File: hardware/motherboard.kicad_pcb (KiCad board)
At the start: 2 copper layers, 200 x 150 mm, 318 parts, among them J1 24 V DC input, J10 AX0: EN, STEP, DIR, GND, J11 AX1: EN, STEP, DIR, GND, J12 General outputs 0-7; pin9 fie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, J13 Encoder 0: +5,A,B,Z,GND, J14 Encoder 1: +5,A,B,Z,GND, J15 Encoder 2: +5,A,B,Z,GND, J16 Keyboard KIN0-7 / KOUT0-7, J17 Keyboard power/reference, J18 I2C0, J19 Full-size SD, SPI, J2 Backlight: +12V, GND, PWM, sw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, J20 ESP-01S socket, J22 LCD LVDS 2x10, 2.00 mm, J24 AI0/GND/AI1/GND/AI2/GND, J25 0-10 V outputs 0-3; pin 1 = c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, J26 Dedicated START button input, J27 Expansion inputs 4-7; 1=GND, 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, J28 AX2: EN, STEP, DIR, GND, J29 AX3: EN, STEP, DIR, GND, J30 AX4: EN, STEP, DIR, GND, J31 Motion AUX open-drain output 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, J32 General outputs 8-15; DO_COM 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, J33 General outputs field +V and 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, J34 PLC positions 5-8 of J7 bank;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, J35 PLC positions 5-8 of J8 bank;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, J4 SWD, J5 Dedicated E-stop loop, J6 Dedicated HOLD button input, J7 PLC inputs 1-8; alternating i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, J8 PLC inputs 9-16; alternating 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, J9 Expansion inputs 0-3; 1=GND, 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, Q5 BSS138, Q6 BSS138, Q7 BSS138, Q8 BSS138, SW2 ESP_PROG, U1 LMR36510ADDAR, U10 74HC595D, U11 74HC595D, U12 74HC595D, U13 74HC595D, U18 LTV-847S, U19 LTV-847S, U2 AMS1117-3.3, U20 LTV-847S, U21 LTV-847S, U24 SN74AHCT541DW, U25 SN74AHCT541DW, U26 ULN2003ADR, U27 ULN2003ADR, U28 SN74AHCT541DW, U3 LMR36510ADDAR, U34 AMS1117-3.3, U35 EL3H7, U36 EL3H7, U37 L78L12ACUTR, U38 TLV2374IDR, U39 EL3H7, U40 TBA2-0512, U41 DS90LV047A, U6 74HC165D, U7 74HC165D, U8 74HC165D, U9 74HC165D

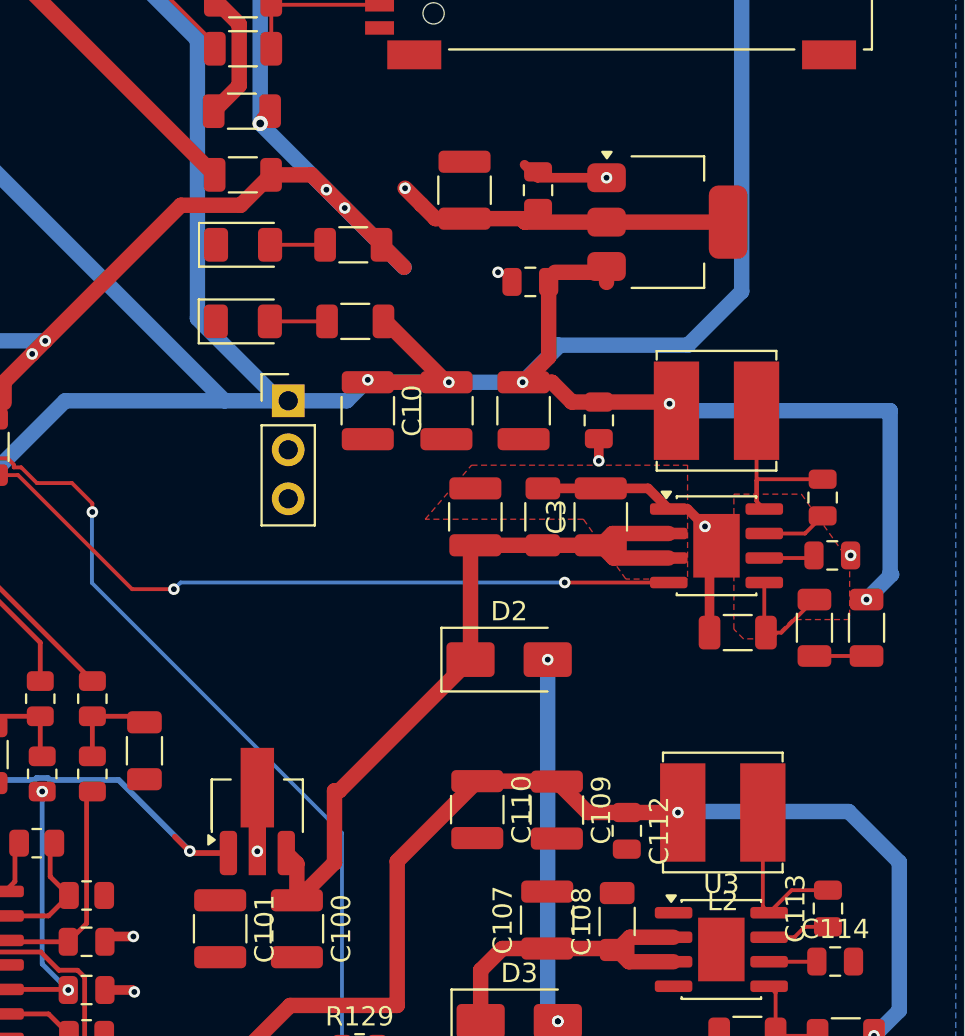
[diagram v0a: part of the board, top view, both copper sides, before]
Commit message: Close final PCB connectivity gaps
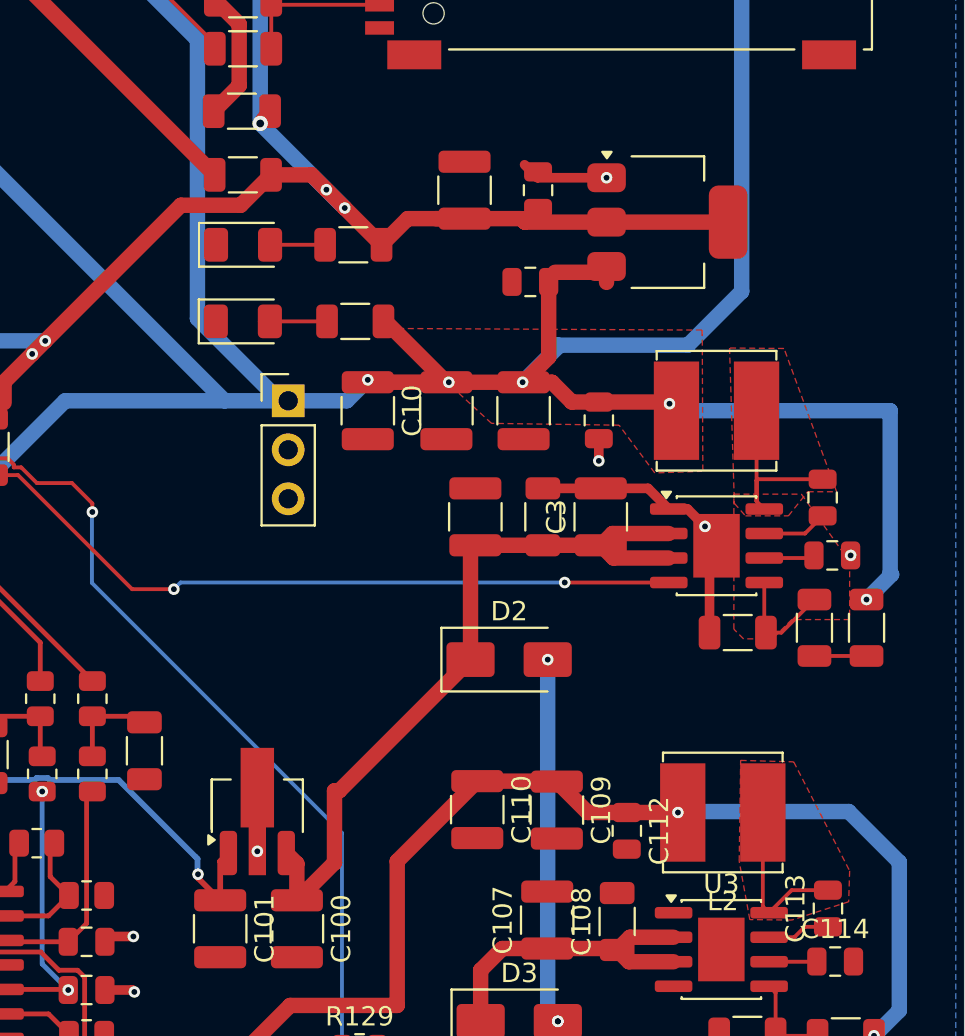
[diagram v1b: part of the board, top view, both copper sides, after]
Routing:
- net +3V3: track 678.7 -> 675.3 mm, vias 29 -> 28
- net +12V_AO: track 26.6 -> 29.4 mm
- net GND: vias 92 -> 91
- added copper zone on F.Cu, net BUCK12_SW
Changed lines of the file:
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@@
 	)
 	(via
-		(at 175.775 93.5)
-		(size 0.6)
-		(drill 0.3)
-		(layers "F.Cu" "B.Cu")
-		(net "GND")
-	)
-	(via
 		(at 157.85 47.9)
 		(size 0.6)
@@
 	)
 	(segment
+		(start 173.225 99.2)
+		(end 177.05 99.2)
+		(width 0.8)
+		(layer "F.Cu")
+		(net "+5V")
+	)
+	(segment
 		(start 173.1 99.2)
 		(end 173.225 99.2)
@@
 	)
 	(segment
-		(start 177.05 99.2)
-		(end 173.225 99.2)
-		(width 0.8)
-		(layer "B.Cu")
-		(net "+5V")
-	)
-	(segment
 		(start 161.6 100.16)
 		(end 153.34 100.16)
@@
 	)
 	(segment
-		(start 159.025 122.75)
-		(end 159.875 123.6)
+		(start 160.225 124.9)
+		(end 161.375 126.05)
 		(width 0.3)
 		(layer "F.Cu")
@@
 	)
 	(segment
-		(start 159.875 123.6)
+		(start 161.375 124.025)
 		(end 161.8 123.6)
 		(width 0.3)
@@
 	)
 	(segment
+		(start 160.225 124.7)
+		(end 160.225 124.9)
+		(width 0.3)
+		(layer "F.Cu")
+		(net "+12V_AO")
+	)
+	(segment
+		(start 161.375 126.05)
+		(end 161.375 124.025)
+		(width 0.3)
+		(layer "F.Cu")
+		(net "+12V_AO")
+	)
+	(segment
 		(start 146.95 123.25)
 		(end 146.95 128.636238)
@@
 	)
 	(via
-		(at 159.8 123.5)
+		(at 160.225 124.7)
 		(size 0.6)
 		(drill 0.3)
@@
 	)
 	(segment
-		(start 151.76005 119.8125)
-		(end 151.86005 119.7125)
+		(start 151.86005 119.7125)
+		(end 152.43995 119.7125)
 		(width 0.3)
 		(layer "B.Cu")
@@
 	)
 	(segment
-		(start 151.86005 119.7125)
-		(end 152.43995 119.7125)
+		(start 160.2 123.9)
+		(end 160.2 124.675)
 		(width 0.3)
 		(layer "B.Cu")
@@
 	)
 	(segment
-		(start 146.8 123.1)
-		(end 150.0875 119.8125)
+		(start 160.1 123.8)
+		(end 160.2 123.9)
+		(width 0.3)
+		(layer "B.Cu")
+		(net "+12V_AO")
+	)
+	(segment
+		(start 151.76005 119.8125)
+		(end 151.86005 119.7125)
+		(width 0.3)
+		(layer "B.Cu")
+		(net "+12V_AO")
+	)
+	(segment
+		(start 150.0875 119.8125)
+		(end 151.76005 119.8125)
 		(width 0.3)
 		(layer "B.Cu")
@@
 	)
 	(segment
+		(start 160.2 124.675)
+		(end 160.225 124.7)
+		(width 0.3)
+		(layer "B.Cu")
+		(net "+12V_AO")
+	)
+	(segment
 		(start 152.43995 119.7125)
 		(end 152.53995 119.8125)
@@
 	)
 	(segment
-		(start 150.0875 119.8125)
-		(end 151.76005 119.8125)
+		(start 156.1125 119.8125)
+		(end 160.1 123.8)
 		(width 0.3)
 		(layer "B.Cu")
@@
 	)
 	(segment
-		(start 156.1125 119.8125)
-		(end 159.725 123.425)
+		(start 146.8 123.1)
+		(end 150.0875 119.8125)
 		(width 0.3)
 		(layer "B.Cu")
@@
 	)
 	(segment
-		(start 170.95625 89.14375)
-		(end 171.80625 89.99375)
-		(width 0.8)
-		(layer "F.Cu")
-		(net "+3V3")
-	)
-	(segment
 		(start 57.25 102.6)
 		(end 57.25 103.25)
@@
 	)
 	(segment
-		(start 170.90625 93.24375)
-		(end 169.7375 92.075)
+		(start 63.325 43.425)
+		(end 63.7 43.05)
 		(width 0.8)
 		(layer "F.Cu")
@@
 	)
 	(segment
-		(start 63.325 43.425)
-		(end 63.7 43.05)
+		(start 174.04 90.72)
+		(end 171.0925 90.72)
 		(width 0.8)
 		(layer "F.Cu")
@@
 	)
 	(segment
+		(start 171.0925 90.72)
+		(end 169.7375 92.075)
+		(width 0.8)
+		(layer "F.Cu")
+		(net "+3V3")
+	)
+	(segment
 		(start 177.175 90.9)
 		(end 177.15 90.875)
@@
 	)
 	(segment
-		(start 172.5325 90.72)
-		(end 171.80625 89.99375)
-		(width 0.8)
-		(layer "F.Cu")
-		(net "+3V3")
-	)
-	(segment
 		(start 57.275 118.2)
 		(end 57.275 117.575)
@@
 	)
 	(via
-		(at 170.95625 89.14375)
-		(size 0.6)
-		(drill 0.3)
-		(layers "F.Cu" "B.Cu")
-		(net "+3V3")
-	)
-	(via
 		(at 134.205 38.775)
 		(size 0.6)
@@
 	)
 	(segment
-		(start 170.90625 93.24375)
-		(end 163.45 85.7875)
-		(width 0.8)
-		(layer "B.Cu")
-		(net "+3V3")
-	)
-	(segment
 		(start 53.585786 57.05)
 		(end 55.45 57.05)
@@
 	)
 	(segment
+		(start 167.83125 90.16875)
+		(end 163.45 85.7875)
+		(width 0.8)
+		(layer "B.Cu")
+		(net "+3V3")
+	)
+	(segment
 		(start 152.30625 97.05625)
 		(end 114.88125 97.05625)
@@
 		(polygon
 			(pts
-				(xy 172 106.3) (xy 174.4 103.5) (xy 185.6 103.5) (xy 185.6 109.4) (xy 182.4 109.4) (xy 180.2 106.3)
+				(xy 175.437495 101.330536) (xy 170.103023 96.410719) (xy 186.359148 96.495993) (xy 186.390896 103.813511)
+				(xy 183.9 103.9) (xy 182.05 101.425)
+			)
+		)
+	)
+	(zone
+		(net "BUCK5_SW")
+		(layer "F.Cu")
+		(hatch edge 0.5)
+		(priority 4)
+		(connect_pads
+			(clearance 0.5)
+		)
+		(min_thickness 0.25)
+		(fill yes
+			(thermal_gap 0.5)
+			(thermal_bridge_width 0.5)
+			(island_removal_mode 0)
+		)
+		(polygon
+			(pts
+				(xy 187.775 97.425) (xy 188.025 105.475) (xy 188.6 106.125) (xy 190.825 106.125) (xy 191.825 104.875)
+				(xy 193.325 104.875) (xy 190.6 97.45)
 			)
 		)
@@
 			)
 		)
+	)
+	(zone
+		(net "BUCK12_SW")
+		(layer "F.Cu")
+		(hatch edge 0.5)
+		(priority 5)
+		(connect_pads
+			(clearance 0.5)
+		)
+		(min_thickness 0.25)
+		(fill yes
+			(thermal_gap 0.5)
+			(thermal_bridge_width 0.5)
+			(island_removal_mode 0)
+		)
+		(polygon
+			(pts
+				(xy 188.35 118.8) (xy 191.1 118.875) (xy 194 124.525) (xy 193.95 126.125) (xy 191 127.075) (xy 188.825 127.05)
+				(xy 188.275 124.025)
+			)
+		)

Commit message: Standardize passives and add microSD alternate
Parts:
- removed R54: 0R, R_1206_3216Metric
- added J36: MicroSD alternative, SPI, microSD_HC_Molex_104031-0811, B.Cu at (189.2, 68.5)
- added JP5: SD_CD_EN, SolderJumper_2_Open_1206Gap, F.Cu at (162.6, 81.9)
- C10, C101, C103, C109, C11, C110, C111, C6, C69, C88, C90: value 22uF 25V -> 22uF 50V
- C92, C94, C96, C98: footprint C_1206_3216Metric -> C_0805_2012Metric
- RN32, RN33, RN34, RN35: value 4x4.7k -> 4x10k
- moved C101 0.35 mm to (161.0, 127.5)
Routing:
- net SD_CD: track 8.26 -> 48.6 mm, vias 0 -> 3
- net SD_DAT2: track 6.99 -> 25.3 mm, vias 0 -> 1
- net SD_DAT1: track 6.23 -> 23.7 mm, vias 0 -> 1
- net SD_CS_N: track 8.43 -> 25.7 mm, vias 0 -> 1
- net SD_MISO: track 9.13 -> 26.3 mm, vias 0 -> 1
- net SD_MOSI: track 8.44 -> 25.0 mm, vias 0 -> 1
- net SD_SCK: track 11.0 -> 24.2 mm, vias 0 -> 1
- net +3V3_SD: track 43.8 -> 56.8 mm, vias 0 -> 1
- net +5V: track 446.2 -> 445.0 mm
- net GND: vias 91 -> 94
